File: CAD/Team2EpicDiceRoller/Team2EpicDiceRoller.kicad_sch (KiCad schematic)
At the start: 62 parts, among them J1 Conn_02x03_Odd_Even, J2 Conn_01x16, J3 Barrel_Jack, Q1 BSS138, SW1 SW_Toggle_SPDT, SW2 Tilt_Switch, SW3 SW_Power, SW4 RotaryEncoder_Switch, SW5 SW_LeftMenu, SW6 SW_MidMenu, SW7 SW_Reset, SW8 SW_RightMenu, U1 MC34063AD, U2 74HC14, U3 MC34063AD, U4 ATmega328P-P, Y1 Crystal_16MHz

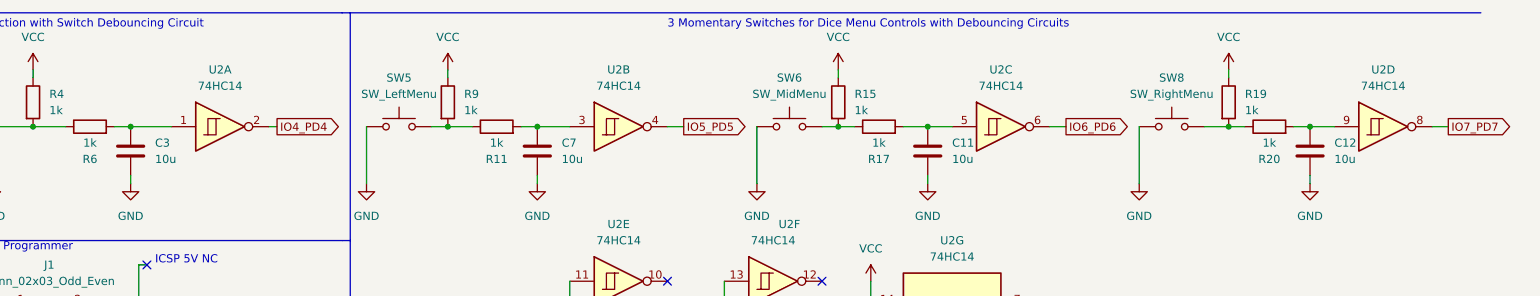
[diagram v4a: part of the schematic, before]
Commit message: Initial routing - done poorly, need to update power switch footprint
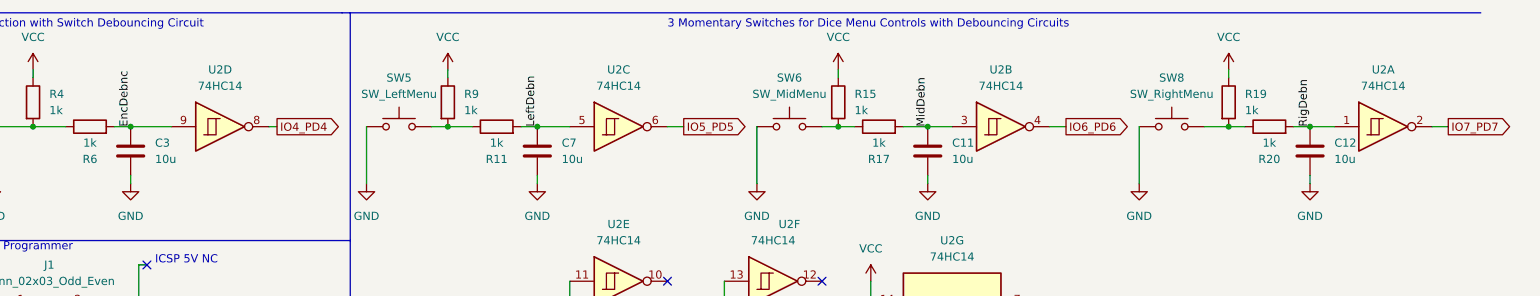
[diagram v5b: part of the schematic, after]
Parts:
- L1, L2: footprint (none) -> Inductor_SMD:L_0805_2012Metric_Pad1.15x1.40mm_HandSolder
- SW2: footprint (none) -> Connector_PinHeader_2.54mm:PinHeader_1x02_P2.54mm_Vertical
- SW3: footprint (none) -> Connector_PinHeader_2.54mm:PinHeader_2x03_P2.54mm_Vertical
- TP1, TP2: footprint (none) -> TestPoint:TestPoint_Pad_D2.0mm
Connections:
- net IO4_PD4: now also U2.8; no longer U2.2
- net IO5_PD5: now also U2.6; no longer U2.4
- net IO6_PD6: now also U2.4; no longer U2.6
- net IO7_PD7: now also U2.2; no longer U2.8
- net LeftDebn: now reaches C7.1, R11.2
- net LeftDebn: now also U2.5; no longer U2.3
- net RigDebn: now reaches C12.1, R20.2
- net RigDebn: now also U2.1; no longer U2.9
- net EncDebnc: now reaches C3.1, R6.2
- net EncDebnc: now also U2.9; no longer U2.1
- net MidDebn: now reaches C11.1, R17.2
- net MidDebn: now also U2.3; no longer U2.5
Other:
- moved on the sheet: U2A, U2B, U2C, U2D
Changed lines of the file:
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@@
     (effects (font (size 1.27 1.27)) (justify left bottom))
   )
+  (label "EncDebnc" (at 67.31 30.48 90)
+    (effects (font (size 1.27 1.27)) (justify left bottom))
+  )
   (label "Vin" (at 72.39 119.38 0)
+    (effects (font (size 1.27 1.27)) (justify left bottom))
+  )
+  (label "LeftDebn" (at 130.81 30.48 90)
+    (effects (font (size 1.27 1.27)) (justify left bottom))
+  )
+  (label "MidDebn" (at 191.77 30.48 90)
+    (effects (font (size 1.27 1.27)) (justify left bottom))
+  )
+  (label "RigDebn" (at 251.46 30.48 90)
     (effects (font (size 1.27 1.27)) (justify left bottom))
   )
@@
       (effects (font (size 1.27 1.27)) (justify left))
     )
-    (property "Footprint" "" (id 2) (at 142.24 165.1 0)
+    (property "Footprint" "TestPoint:TestPoint_Pad_D2.0mm" (id 2) (at 142.24 165.1 0)
       (effects (font (size 1.27 1.27)) hide)
     )
@@
       (effects (font (size 1.27 1.27)) (justify left))
     )
-    (property "Footprint" "" (id 2) (at 147.32 128.27 0)
+    (property "Footprint" "TestPoint:TestPoint_Pad_D2.0mm" (id 2) (at 147.32 128.27 0)
       (effects (font (size 1.27 1.27)) hide)
     )
@@
     (property "Reference" "L1" (id 0) (at 88.9 160.02 90))
     (property "Value" "100u" (id 1) (at 88.9 162.56 90))
-    (property "Footprint" "" (id 2) (at 88.9 166.37 0)
+    (property "Footprint" "Inductor_SMD:L_0805_2012Metric_Pad1.15x1.40mm_HandSolder" (id 2) (at 88.9 166.37 0)
       (effects (font (size 1.27 1.27)) hide)
     )
@@
     (property "Reference" "L2" (id 0) (at 129.54 123.19 90))
     (property "Value" "100u" (id 1) (at 129.54 125.73 90))
-    (property "Footprint" "" (id 2) (at 129.54 129.54 0)
+    (property "Footprint" "Inductor_SMD:L_0805_2012Metric_Pad1.15x1.40mm_HandSolder" (id 2) (at 129.54 129.54 0)
       (effects (font (size 1.27 1.27)) hide)
     )
@@
     (property "Reference" "SW3" (id 0) (at 26.67 149.86 0))
     (property "Value" "SW_Power" (id 1) (at 26.67 152.4 0))
-    (property "Footprint" "" (id 2) (at 26.67 156.21 0)
+    (property "Footprint" "Connector_PinHeader_2.54mm:PinHeader_2x03_P2.54mm_Vertical" (id 2) (at 26.67 156.21 0)
       (effects (font (size 1.27 1.27)) hide)
     )
@@
     (property "Reference" "SW2" (id 0) (at 24.13 80.01 0))
     (property "Value" "Tilt_Switch" (id 1) (at 24.13 82.55 0))
-    (property "Footprint" "" (id 2) (at 24.13 87.63 0)
+    (property "Footprint" "Connector_PinHeader_2.54mm:PinHeader_1x02_P2.54mm_Vertical" (id 2) (at 24.13 87.63 0)
       (effects (font (size 1.27 1.27)) hide)
     )
@@
     (pin "2")
   )
-  (symbol (lib_id "74xx:74HC14") (at 81.28 30.48 0) (unit 1)
+  (symbol (lib_id "74xx:74HC14") (at 81.28 30.48 0) (unit 4)
     (in_bom yes) (on_board yes) (fields_autoplaced)
     (property "Reference" "U2" (id 0) (at 81.28 21.59 0))
@@
       (effects (font (size 1.27 1.27)) hide)
     )
-    (pin "1")
-    (pin "2")
-  )
-  (symbol (lib_id "74xx:74HC14") (at 143.51 30.48 0) (unit 2)
+    (pin "8")
+    (pin "9")
+  )
+  (symbol (lib_id "74xx:74HC14") (at 143.51 30.48 0) (unit 3)
     (in_bom yes) (on_board yes) (fields_autoplaced)
     (property "Reference" "U2" (id 0) (at 143.51 21.59 0))
@@
       (effects (font (size 1.27 1.27)) hide)
     )
-    (pin "3")
-    (pin "4")
+    (pin "5")
+    (pin "6")
   )
   (symbol (lib_id "74xx:74HC14") (at 143.51 54.61 0) (unit 5)
@@
     (pin "13")
   )
-  (symbol (lib_id "74xx:74HC14") (at 203.2 30.48 0) (unit 3)
+  (symbol (lib_id "74xx:74HC14") (at 203.2 30.48 0) (unit 2)
     (in_bom yes) (on_board yes) (fields_autoplaced)
     (property "Reference" "U2" (id 0) (at 203.2 21.59 0))
@@
       (effects (font (size 1.27 1.27)) hide)
     )
-    (pin "5")
-    (pin "6")
-  )
-  (symbol (lib_id "74xx:74HC14") (at 262.89 30.48 0) (unit 4)
+    (pin "3")
+    (pin "4")
+  )
+  (symbol (lib_id "74xx:74HC14") (at 262.89 30.48 0) (unit 1)
     (in_bom yes) (on_board yes) (fields_autoplaced)
     (property "Reference" "U2" (id 0) (at 262.89 21.59 0))
@@
       (effects (font (size 1.27 1.27)) hide)
     )
-    (pin "8")
-    (pin "9")
+    (pin "1")
+    (pin "2")
   )
   (symbol (lib_id "Device:RotaryEncoder_Switch") (at 36.83 33.02 0) (unit 1)
@@
     )
     (path "/efd78667-ad9c-4abe-95be-41cfe7b3f9a2"
-      (reference "L1") (unit 1) (value "100u") (footprint "")
+      (reference "L1") (unit 1) (value "100u") (footprint "Inductor_SMD:L_0805_2012Metric_Pad1.15x1.40mm_HandSolder")
     )
     (path "/73ef3769-79c6-46fb-8bea-7fdb20560c7d"
-      (reference "L2") (unit 1) (value "100u") (footprint "")
+      (reference "L2") (unit 1) (value "100u") (footprint "Inductor_SMD:L_0805_2012Metric_Pad1.15x1.40mm_HandSolder")
     )
     (path "/08460420-b30b-45a0-968d-ea36b360168a"
@@
     )
     (path "/a94b1b9e-64b4-4337-907b-28f328893b5b"
-      (reference "SW2") (unit 1) (value "Tilt_Switch") (footprint "")
+      (reference "SW2") (unit 1) (value "Tilt_Switch") (footprint "Connector_PinHeader_2.54mm:PinHeader_1x02_P2.54mm_Vertical")
     )
     (path "/62decbfd-9b39-4533-9afd-2a303a856754"
-      (reference "SW3") (unit 1) (value "SW_Power") (footprint "")
+      (reference "SW3") (unit 1) (value "SW_Power") (footprint "Connector_PinHeader_2.54mm:PinHeader_2x03_P2.54mm_Vertical")
     )
     (path "/09f16ce9-bd04-40ee-92ae-f355745771f9"
@@
     )
     (path "/7d1ff827-9479-427e-852e-01ec466ff6f9"
-      (reference "TP1") (unit 1) (value "TestPoint") (footprint "")
+      (reference "TP1") (unit 1) (value "TestPoint") (footprint "TestPoint:TestPoint_Pad_D2.0mm")
     )
     (path "/9423c47e-8566-4af8-ad8a-b85648689249"
-      (reference "TP2") (unit 1) (value "TestPoint") (footprint "")
+      (reference "TP2") (unit 1) (value "TestPoint") (footprint "TestPoint:TestPoint_Pad_D2.0mm")
     )
     (path "/6ac96d5f-5167-47fa-b9d4-15bdec4bb4fd"

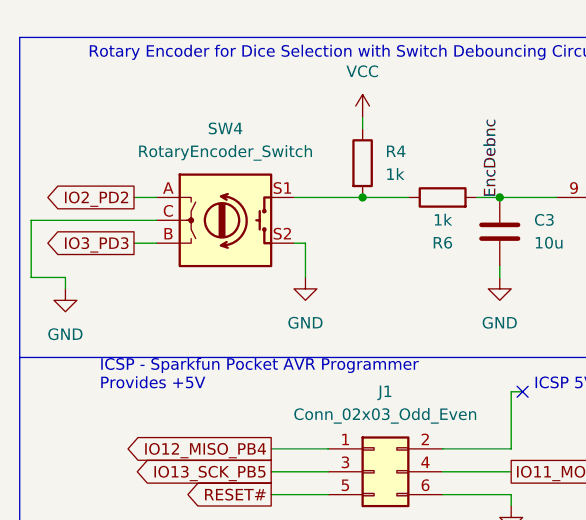
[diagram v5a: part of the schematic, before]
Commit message: Updated schematic to remove traces and update the footprints
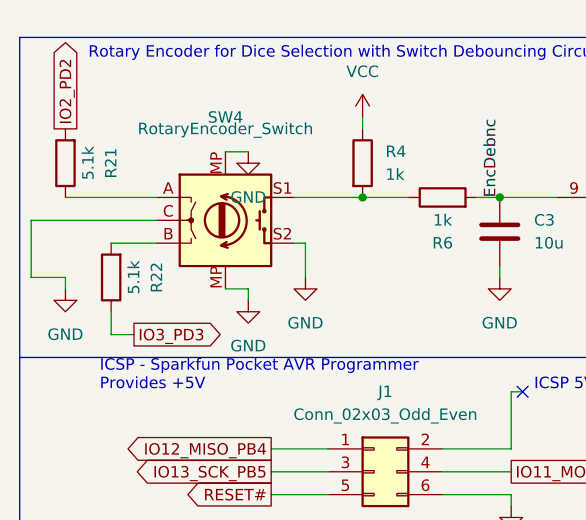
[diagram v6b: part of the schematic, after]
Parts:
- added R21, R22: 5.1k, Resistor_SMD:R_1206_3216Metric_Pad1.30x1.75mm_HandSolder, symbol Device:R
- SW3: footprint Connector_PinHeader_2.54mm:PinHeader_2x03_P2.54mm_Vertical -> GF-123-0054:SW_GF-123-0054
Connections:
- net GND: now also SW4.MP
- net IO2_PD2: now also R21.2; no longer SW4.A
- net IO3_PD3: now also R22.1; no longer SW4.B
- new net: R22.2, SW4.B
- new net: R21.1, SW4.A
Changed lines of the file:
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@@
     (stroke (width 0) (type default) (color 0 0 0 0))
   )
+  (wire (pts (xy 19.05 30.48) (xy 29.21 30.48))
+    (stroke (width 0) (type default) (color 0 0 0 0))
+  )
   (wire (pts (xy 19.05 39.37) (xy 19.05 40.64))
     (stroke (width 0) (type default) (color 0 0 0 0))
@@
     (stroke (width 0) (type default) (color 0 0 0 0))
   )
-  (wire (pts (xy 26.67 30.48) (xy 29.21 30.48))
+  (wire (pts (xy 24.13 35.56) (xy 29.21 35.56))
+    (stroke (width 0) (type default) (color 0 0 0 0))
+  )
+  (wire (pts (xy 24.13 43.18) (xy 24.13 45.72))
     (stroke (width 0) (type default) (color 0 0 0 0))
   )
-  (wire (pts (xy 26.67 35.56) (xy 29.21 35.56))
+  (wire (pts (xy 24.13 45.72) (xy 26.67 45.72))
     (stroke (width 0) (type default) (color 0 0 0 0))
   )
@@
     (stroke (width 0) (type default) (color 0 0 0 0))
   )
+  (wire (pts (xy 36.83 25.4) (xy 39.37 25.4))
+    (stroke (width 0) (type default) (color 0 0 0 0))
+  )
+  (wire (pts (xy 36.83 40.64) (xy 39.37 40.64))
+    (stroke (width 0) (type default) (color 0 0 0 0))
+  )
   (wire (pts (xy 38.1 111.76) (xy 38.1 120.65))
     (stroke (width 0) (type default) (color 0 0 0 0))
@@
     (stroke (width 0) (type default) (color 0 0 0 0))
   )
+  (wire (pts (xy 39.37 40.64) (xy 39.37 41.91))
+    (stroke (width 0) (type default) (color 0 0 0 0))
+  )
   (wire (pts (xy 39.37 144.78) (xy 39.37 156.21))
     (stroke (width 0) (type default) (color 0 0 0 0))
@@
     (effects (font (size 1.27 1.27)) (justify left bottom))
   )
-  (global_label "IO2_PD2" (shape output) (at 26.67 30.48 180) (fields_autoplaced)
-    (effects (font (size 1.27 1.27)) (justify right))
-    (property "Intersheet References" "${INTERSHEET_REFS}" (id 0) (at 16.395 30.4006 0)
-      (effects (font (size 1.27 1.27)) (justify right) hide)
+  (global_label "IO2_PD2" (shape output) (at 19.05 22.86 90) (fields_autoplaced)
+    (effects (font (size 1.27 1.27)) (justify left))
+    (property "Intersheet References" "${INTERSHEET_REFS}" (id 0) (at 19.1294 12.585 90)
+      (effects (font (size 1.27 1.27)) (justify left) hide)
     )
   )
-  (global_label "IO3_PD3" (shape output) (at 26.67 35.56 180) (fields_autoplaced)
-    (effects (font (size 1.27 1.27)) (justify right))
-    (property "Intersheet References" "${INTERSHEET_REFS}" (id 0) (at 16.395 35.4806 0)
-      (effects (font (size 1.27 1.27)) (justify right) hide)
+  (global_label "IO3_PD3" (shape output) (at 26.67 45.72 0) (fields_autoplaced)
+    (effects (font (size 1.27 1.27)) (justify left))
+    (property "Intersheet References" "${INTERSHEET_REFS}" (id 0) (at 36.945 45.7994 0)
+      (effects (font (size 1.27 1.27)) (justify left) hide)
     )
   )
@@
     (pin "1")
   )
+  (symbol (lib_id "power:GND") (at 39.37 25.4 0) (unit 1)
+    (in_bom yes) (on_board yes) (fields_autoplaced)
+    (property "Reference" "#PWR0102" (id 0) (at 39.37 31.75 0)
+      (effects (font (size 1.27 1.27)) hide)
+    )
+    (property "Value" "GND" (id 1) (at 39.37 30.48 0))
+    (property "Footprint" "" (id 2) (at 39.37 25.4 0)
+      (effects (font (size 1.27 1.27)) hide)
+    )
+    (property "Datasheet" "" (id 3) (at 39.37 25.4 0)
+      (effects (font (size 1.27 1.27)) hide)
+    )
+    (pin "1")
+  )
+  (symbol (lib_id "power:GND") (at 39.37 41.91 0) (unit 1)
+    (in_bom yes) (on_board yes) (fields_autoplaced)
+    (property "Reference" "#PWR0101" (id 0) (at 39.37 48.26 0)
+      (effects (font (size 1.27 1.27)) hide)
+    )
+    (property "Value" "GND" (id 1) (at 39.37 46.99 0))
+    (property "Footprint" "" (id 2) (at 39.37 41.91 0)
+      (effects (font (size 1.27 1.27)) hide)
+    )
+    (property "Datasheet" "" (id 3) (at 39.37 41.91 0)
+      (effects (font (size 1.27 1.27)) hide)
+    )
+    (pin "1")
+  )
   (symbol (lib_id "power:GND") (at 39.37 176.53 0) (unit 1)
     (in_bom yes) (on_board yes) (fields_autoplaced)
@@
     (pin "2")
   )
+  (symbol (lib_id "Device:R") (at 19.05 26.67 180) (unit 1)
+    (in_bom yes) (on_board yes)
+    (property "Reference" "R21" (id 0) (at 24.13 26.67 90))
+    (property "Value" "5.1k" (id 1) (at 21.59 26.67 90))
+    (property "Footprint" "Resistor_SMD:R_1206_3216Metric_Pad1.30x1.75mm_HandSolder" (id 2) (at 20.828 26.67 90)
+      (effects (font (size 1.27 1.27)) hide)
+    )
+    (property "Datasheet" "~" (id 3) (at 19.05 26.67 0)
+      (effects (font (size 1.27 1.27)) hide)
+    )
+    (pin "1")
+    (pin "2")
+  )
+  (symbol (lib_id "Device:R") (at 24.13 39.37 180) (unit 1)
+    (in_bom yes) (on_board yes)
+    (property "Reference" "R22" (id 0) (at 29.21 39.37 90))
+    (property "Value" "5.1k" (id 1) (at 26.67 39.37 90))
+    (property "Footprint" "Resistor_SMD:R_1206_3216Metric_Pad1.30x1.75mm_HandSolder" (id 2) (at 25.908 39.37 90)
+      (effects (font (size 1.27 1.27)) hide)
+    )
+    (property "Datasheet" "~" (id 3) (at 24.13 39.37 0)
+      (effects (font (size 1.27 1.27)) hide)
+    )
+    (pin "1")
+    (pin "2")
+  )
   (symbol (lib_id "Device:R") (at 35.56 81.28 0) (unit 1)
     (in_bom yes) (on_board yes) (fields_autoplaced)
@@
     (property "Reference" "SW3" (id 0) (at 26.67 149.86 0))
     (property "Value" "SW_Power" (id 1) (at 26.67 152.4 0))
-    (property "Footprint" "Connector_PinHeader_2.54mm:PinHeader_2x03_P2.54mm_Vertical" (id 2) (at 26.67 156.21 0)
+    (property "Footprint" "GF-123-0054:SW_GF-123-0054" (id 2) (at 26.67 156.21 0)
       (effects (font (size 1.27 1.27)) hide)
     )
@@
     (pin "2")
   )
-  (symbol (lib_id "Device:RotaryEncoder_Switch") (at 36.83 33.02 0) (unit 1)
+  (symbol (lib_name "RotaryEncoder_Switch_1") (lib_id "Device:RotaryEncoder_Switch") (at 36.83 33.02 0) (unit 1)
     (in_bom yes) (on_board yes) (fields_autoplaced)
-    (property "Reference" "SW4" (id 0) (at 36.83 22.86 0))
-    (property "Value" "RotaryEncoder_Switch" (id 1) (at 36.83 25.4 0))
+    (property "Reference" "SW4" (id 0) (at 36.83 21.59 0))
+    (property "Value" "RotaryEncoder_Switch" (id 1) (at 36.83 22.86 0))
     (property "Footprint" "Rotary_Encoder:RotaryEncoder_Alps_EC11E-Switch_Vertical_H20mm" (id 2) (at 33.02 28.956 0)
       (effects (font (size 1.27 1.27)) hide)
@@
     (pin "B")
     (pin "C")
+    (pin "MP")
+    (pin "MP")
     (pin "S1")
     (pin "S2")
@@
       (reference "#PWR055") (unit 1) (value "GND") (footprint "")
     )
+    (path "/869f3aca-f654-4ae7-9fc3-d57e12452789"
+      (reference "#PWR0101") (unit 1) (value "GND") (footprint "")
+    )
+    (path "/20074d8d-cd66-4113-b96f-8eadcf58cf99"
+      (reference "#PWR0102") (unit 1) (value "GND") (footprint "")
+    )
     (path "/0d231509-68f0-4212-ae79-6549c7a4a82b"
       (reference "C1") (unit 1) (value "100u") (footprint "Capacitor_SMD:C_1206_3216Metric_Pad1.33x1.80mm_HandSolder")
@@
       (reference "R20") (unit 1) (value "1k") (footprint "Resistor_SMD:R_1206_3216Metric_Pad1.30x1.75mm_HandSolder")
     )
+    (path "/516f2a99-092c-455c-a331-68b17104f70d"
+      (reference "R21") (unit 1) (value "5.1k") (footprint "Resistor_SMD:R_1206_3216Metric_Pad1.30x1.75mm_HandSolder")
+    )
+    (path "/20752432-6024-421e-a5a6-ec2a575a81cd"
+      (reference "R22") (unit 1) (value "5.1k") (footprint "Resistor_SMD:R_1206_3216Metric_Pad1.30x1.75mm_HandSolder")
+    )
     (path "/daa876e5-5262-45eb-8eaa-bc6937395761"
       (reference "RV1") (unit 1) (value "5k") (footprint "Library:TRIM_TC33X-2-502E")
@@
     )
     (path "/62decbfd-9b39-4533-9afd-2a303a856754"
-      (reference "SW3") (unit 1) (value "SW_Power") (footprint "Connector_PinHeader_2.54mm:PinHeader_2x03_P2.54mm_Vertical")
+      (reference "SW3") (unit 1) (value "SW_Power") (footprint "GF-123-0054:SW_GF-123-0054")
     )
-    (path "/09f16ce9-bd04-40ee-92ae-f355745771f9"
+    (path "/c14e2302-7a1a-4a4a-b312-326f08bc623f"
       (reference "SW4") (unit 1) (value "RotaryEncoder_Switch") (footprint "Rotary_Encoder:RotaryEncoder_Alps_EC11E-Switch_Vertical_H20mm")
     )
